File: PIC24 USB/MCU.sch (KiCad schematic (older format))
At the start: 12 parts, among them U1 PIC24FJXXXGB106, X1 CRYSTAL_12MHZ

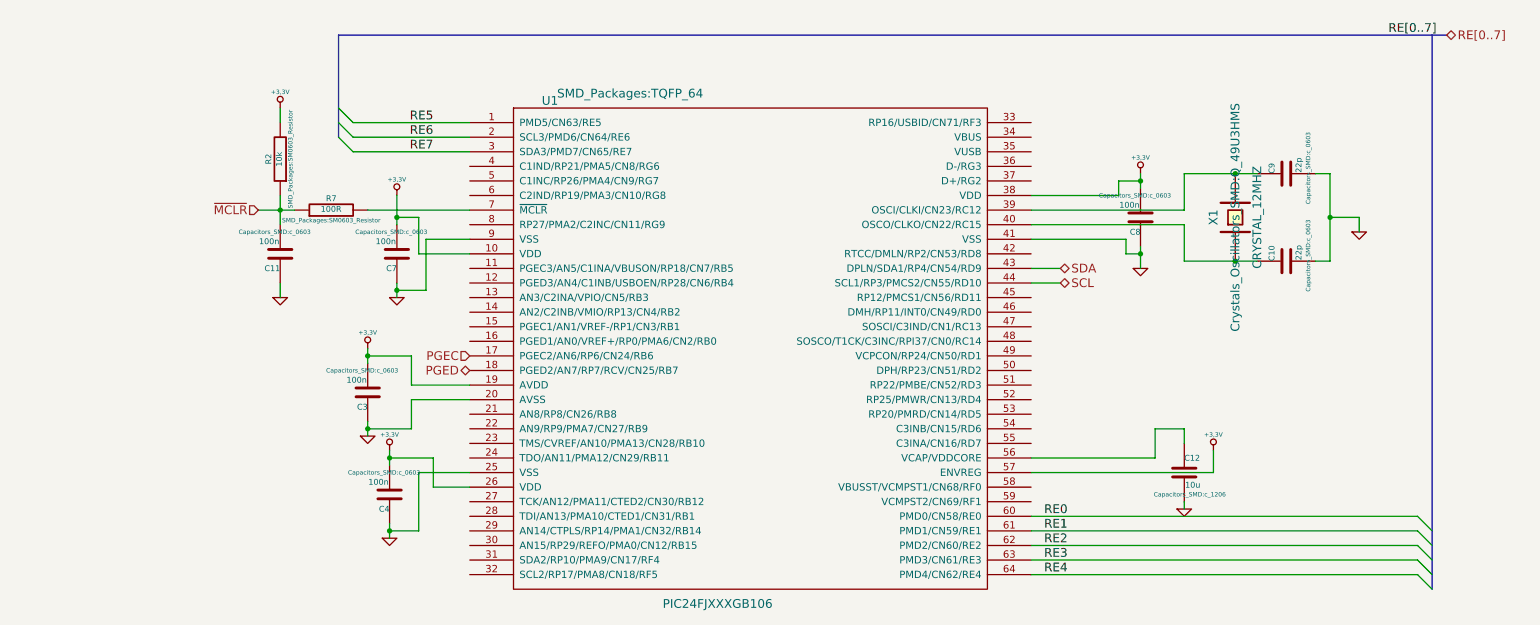
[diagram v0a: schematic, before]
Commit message: added led display, many additional headers and DAC
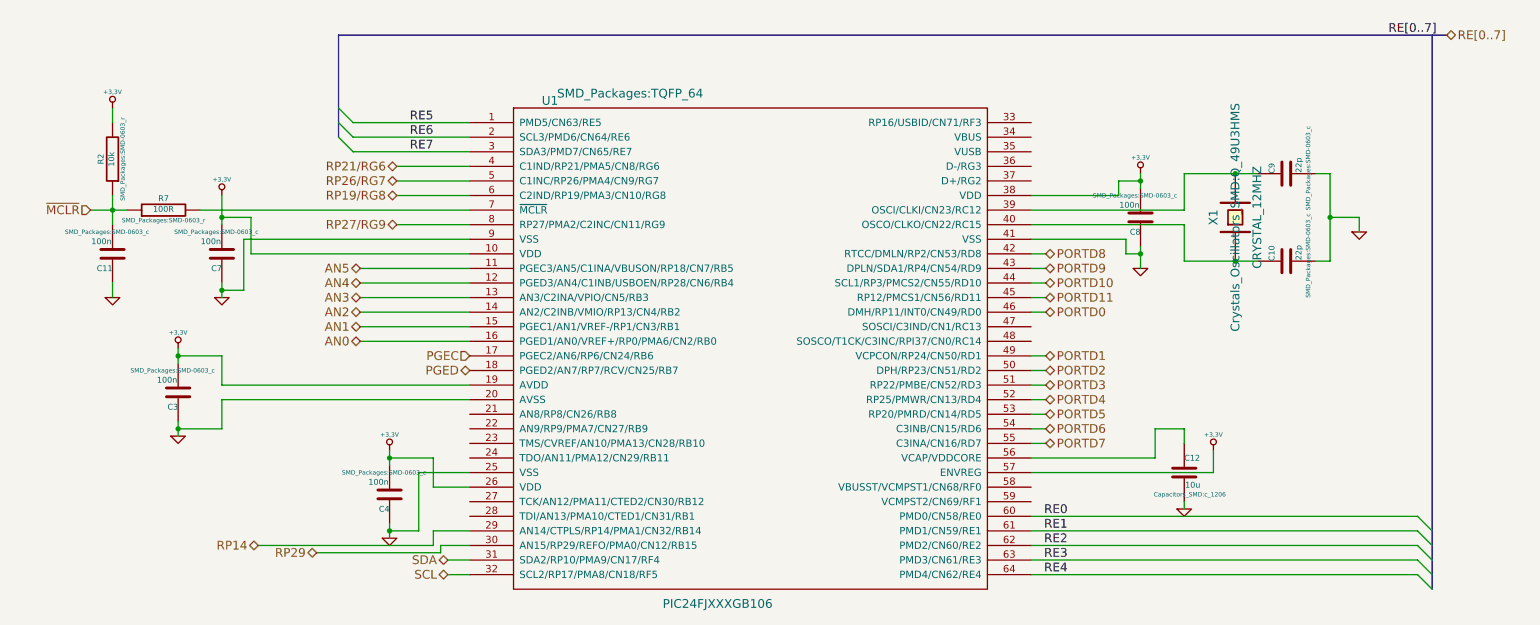
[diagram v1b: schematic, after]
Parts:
- C10, C11, C3, C4, C7, C8, C9: footprint Capacitors_SMD:c_0603 -> SMD_Packages:SMD-0603_c
- R2, R7: footprint SMD_Packages:SM0603_Resistor -> SMD_Packages:SMD-0603_r
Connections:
- net SCL: now also U1.32 (SCL2/RP17/PMA8/CN18/RF5); no longer U1.44 (SCL1/RP3/PMCS2/CN55/RD10)
- net SDA: now also U1.31 (SDA2/RP10/PMA9/CN17/RF4); no longer U1.43 (DPLN/SDA1/RP4/CN54/RD9)
- net AN5: now reaches U1.11 (PGEC3/AN5/C1INA/VBUSON/RP18/CN7/RB5)
- net AN4: now reaches U1.12 (PGED3/AN4/C1INB/USBOEN/RP28/CN6/RB4)
- net AN3: now reaches U1.13 (AN3/C2INA/VPIO/CN5/RB3)
- net AN2: now reaches U1.14 (AN2/C2INB/VMIO/RP13/CN4/RB2)
- net AN1: now reaches U1.15 (PGEC1/AN1/VREF-/RP1/CN3/RB1)
- net AN0: now reaches U1.16 (PGED1/AN0/VREF+/RP0/PMA6/CN2/RB0)
- net RP14: now reaches U1.29 (AN14/CTPLS/RP14/PMA1/CN32/RB14)
- net RP29: now reaches U1.30 (AN15/RP29/REFO/PMA0/CN12/RB15)
- net RP21/RG6: now reaches U1.4 (C1IND/RP21/PMA5/CN8/RG6)
- net PORTD8: now reaches U1.42 (RTCC/DMLN/RP2/CN53/RD8)
- net PORTD11: now reaches U1.45 (RP12/PMCS1/CN56/RD11)
- net PORTD0: now reaches U1.46 (DMH/RP11/INT0/CN49/RD0)
- net PORTD1: now reaches U1.49 (VCPCON/RP24/CN50/RD1)
- net RP26/RG7: now reaches U1.5 (C1INC/RP26/PMA4/CN9/RG7)
- net PORTD2: now reaches U1.50 (DPH/RP23/CN51/RD2)
- net PORTD3: now reaches U1.51 (RP22/PMBE/CN52/RD3)
- net PORTD4: now reaches U1.52 (RP25/PMWR/CN13/RD4)
- net PORTD5: now reaches U1.53 (RP20/PMRD/CN14/RD5)
- net PORTD6: now reaches U1.54 (C3INB/CN15/RD6)
- net PORTD7: now reaches U1.55 (C3INA/CN16/RD7)
- net RP19/RG8: now reaches U1.6 (C2IND/RP19/PMA3/CN10/RG8)
- net RP27/RG9: now reaches U1.8 (RP27/PMA2/C2INC/CN11/RG9)
- new net PORTD10: U1.44 (SCL1/RP3/PMCS2/CN55/RD10)
- new net PORTD9: U1.43 (DPLN/SDA1/RP4/CN54/RD9)
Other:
- moved on the sheet: C11, C3, C7, R2, R7

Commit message: more hierarchical pin for MCU section, connected USB lines in schematic
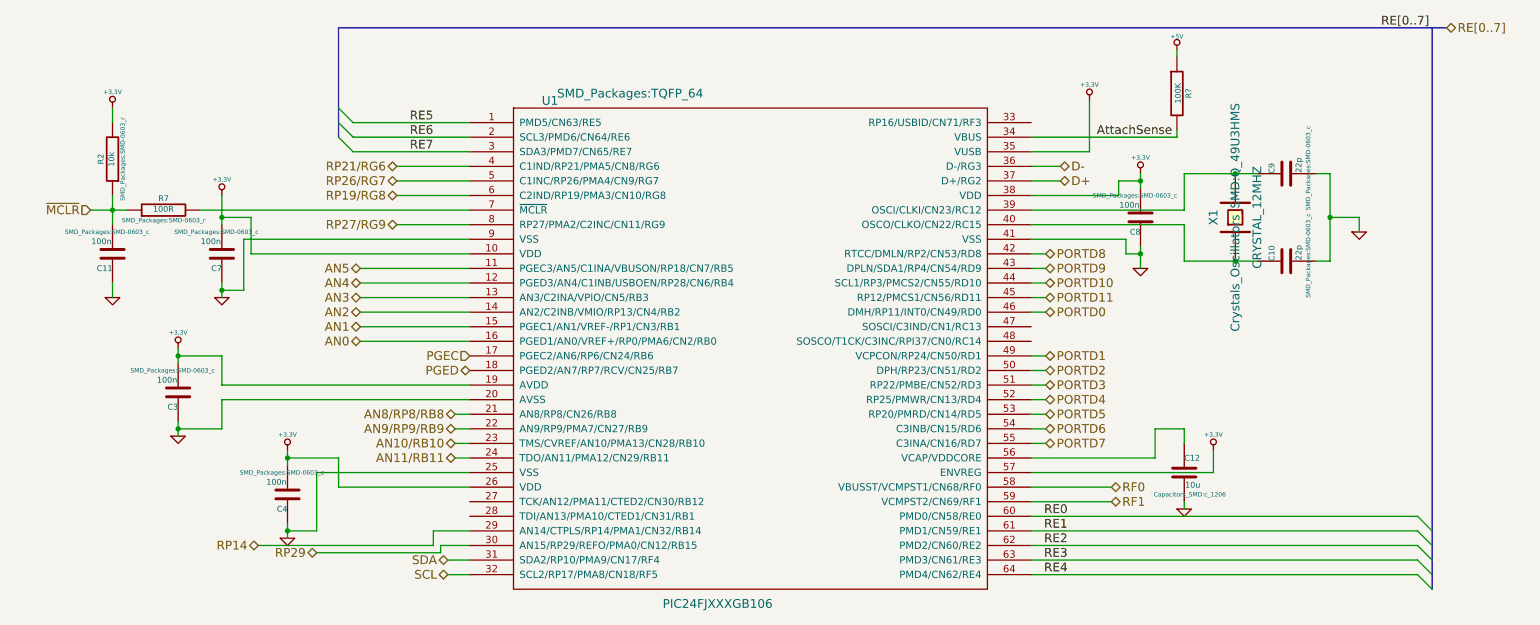
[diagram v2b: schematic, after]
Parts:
- added R?: 100K, symbol R
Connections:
- net +3.3V: now also U1.35 (VUSB)
- net AN8/RP8/RB8: now reaches U1.21 (AN8/RP8/CN26/RB8)
- net AN9/RP9/RB9: now reaches U1.22 (AN9/RP9/PMA7/CN27/RB9)
- net AN10/RB10: now reaches U1.23 (TMS/CVREF/AN10/PMA13/CN28/RB10)
- net AN11/RB11: now reaches U1.24 (TDO/AN11/PMA12/CN29/RB11)
- net AttachSense: now reaches U1.34 (VBUS)
- net AttachSense: now also R?.2
- net D-: now reaches U1.36 (D-/RG3)
- net D+: now reaches U1.37 (D+/RG2)
- net RF0: now reaches U1.58 (VBUSST/VCMPST1/CN68/RF0)
- net RF1: now reaches U1.59 (VCMPST2/CN69/RF1)
- new net +5V: R?.1
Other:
- moved on the sheet: C4

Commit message: connected SPI DAC
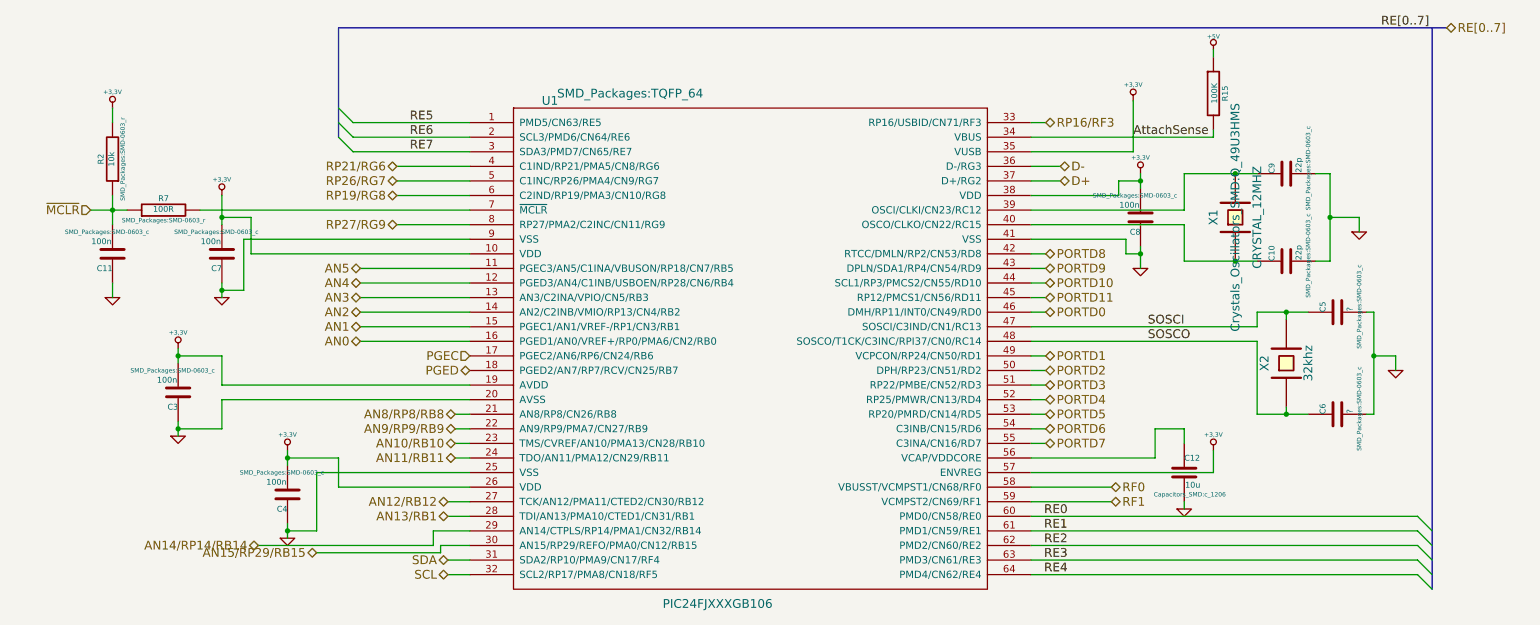
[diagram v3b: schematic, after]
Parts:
- added C5, C6: ?, SMD_Packages:SMD-0603_c, symbol C
- added X2: 32khz, symbol CRYSTAL
- gave numbers to parts that had none: 1
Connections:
- net AttachSense is gone; now on net +3.3V: R15.2, U1.34 (VBUS)
- net GND: now also C5.2, C6.2
- net AN12/RB12: now reaches U1.27 (TCK/AN12/PMA11/CTED2/CN30/RB12)
- net AN13/RB1: now reaches U1.28 (TDI/AN13/PMA10/CTED1/CN31/RB1)
- net RP16/RF3: now reaches U1.33 (RP16/USBID/CN71/RF3)
- net SOSCI: now reaches U1.47 (SOSCI/C3IND/CN1/RC13)
- net SOSCI: now also C5.1, X2.2
- net SOSCO: now reaches U1.48 (SOSCO/T1CK/C3INC/RPI37/CN0/RC14)
- net SOSCO: now also C6.1, X2.1
- net RP14 renamed AN14/RP14/RB14
- net RP29 renamed AN15/RP29/RB15
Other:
- moved on the sheet: R15
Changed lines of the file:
@@
 $Descr A4 11693 8268
 encoding utf-8
-Sheet 2 3
+Sheet 3 3
 Title ""
 Date "3 aug 2014"
@@
 ~MCLR
 $Comp
-L GND #PWR035
+L GND #PWR47
 U 1 1 53DA26E1
 P 1750 3500
-F 0 "#PWR035" H 1750 3500 30  0001 C CNN
+F 0 "#PWR47" H 1750 3500 30  0001 C CNN
 F 1 "GND" H 1750 3430 30  0001 C CNN
 F 2 "" H 1750 3500 60  0000 C CNN
@@
 $EndComp
 $Comp
-L GND #PWR036
+L GND #PWR49
 U 1 1 53DA26EE
 P 2200 5150
-F 0 "#PWR036" H 2200 5150 30  0001 C CNN
+F 0 "#PWR49" H 2200 5150 30  0001 C CNN
 F 1 "GND" H 2200 5080 30  0001 C CNN
 F 2 "" H 2200 5150 60  0000 C CNN
@@
 $EndComp
 $Comp
-L GND #PWR037
+L GND #PWR52
 U 1 1 53DA26F4
 P 8050 3300
-F 0 "#PWR037" H 8050 3300 30  0001 C CNN
+F 0 "#PWR52" H 8050 3300 30  0001 C CNN
 F 1 "GND" H 8050 3230 30  0001 C CNN
 F 2 "" H 8050 3300 60  0000 C CNN
@@
 $EndComp
 $Comp
-L +3,3V #PWR038
+L +3,3V #PWR51
 U 1 1 53DA2840
 P 8050 2650
-F 0 "#PWR038" H 8050 2610 30  0001 C CNN
+F 0 "#PWR51" H 8050 2610 30  0001 C CNN
 F 1 "+3,3V" H 8050 2760 30  0000 C CNN
 F 2 "" H 8050 2650 60  0000 C CNN
@@
 $EndComp
 $Comp
-L +3,3V #PWR039
+L +3,3V #PWR46
 U 1 1 53DA284D
 P 1750 2800
-F 0 "#PWR039" H 1750 2760 30  0001 C CNN
+F 0 "#PWR46" H 1750 2760 30  0001 C CNN
 F 1 "+3,3V" H 1750 2910 30  0000 C CNN
 F 2 "" H 1750 2800 60  0000 C CNN
@@
 $EndComp
 $Comp
-L +3,3V #PWR040
+L +3,3V #PWR48
 U 1 1 53DA2853
 P 2200 4550
-F 0 "#PWR040" H 2200 4510 30  0001 C CNN
+F 0 "#PWR48" H 2200 4510 30  0001 C CNN
 F 1 "+3,3V" H 2200 4660 30  0000 C CNN
 F 2 "" H 2200 4550 60  0000 C CNN
@@
 $EndComp
 $Comp
-L +3,3V #PWR041
+L +3,3V #PWR44
 U 1 1 53DA2865
 P 1450 3850
-F 0 "#PWR041" H 1450 3810 30  0001 C CNN
+F 0 "#PWR44" H 1450 3810 30  0001 C CNN
 F 1 "+3,3V" H 1450 3960 30  0000 C CNN
 F 2 "" H 1450 3850 60  0000 C CNN
@@
 $EndComp
 $Comp
-L GND #PWR042
+L GND #PWR56
 U 1 1 53DA331F
 P 9550 3050
-F 0 "#PWR042" H 9550 3050 30  0001 C CNN
+F 0 "#PWR56" H 9550 3050 30  0001 C CNN
 F 1 "GND" H 9550 2980 30  0001 C CNN
 F 2 "" H 9550 3050 60  0000 C CNN
@@
 $EndComp
 $Comp
-L GND #PWR043
+L GND #PWR45
 U 1 1 53DA3460
 P 1450 4450
-F 0 "#PWR043" H 1450 4450 30  0001 C CNN
+F 0 "#PWR45" H 1450 4450 30  0001 C CNN
 F 1 "GND" H 1450 4380 30  0001 C CNN
 F 2 "" H 1450 4450 60  0000 C CNN
@@
 RE4
 $Comp
-L +3,3V #PWR044
+L +3,3V #PWR55
 U 1 1 53DBFFDE
 P 8550 4550
-F 0 "#PWR044" H 8550 4510 30  0001 C CNN
+F 0 "#PWR55" H 8550 4510 30  0001 C CNN
 F 1 "+3,3V" H 8550 4660 30  0000 C CNN
 F 2 "" H 8550 4550 60  0000 C CNN
@@
 $EndComp
 $Comp
-L GND #PWR045
+L GND #PWR53
 U 1 1 53DC0153
 P 8350 4950
-F 0 "#PWR045" H 8350 4950 30  0001 C CNN
+F 0 "#PWR53" H 8350 4950 30  0001 C CNN
 F 1 "GND" H 8350 4880 30  0001 C CNN
 F 2 "" H 8350 4950 60  0000 C CNN
@@
 $EndComp
 $Comp
-L GND #PWR046
+L GND #PWR43
 U 1 1 53DEB25D
 P 1000 3500
-F 0 "#PWR046" H 1000 3500 30  0001 C CNN
+F 0 "#PWR43" H 1000 3500 30  0001 C CNN
 F 1 "GND" H 1000 3430 30  0001 C CNN
 F 2 "" H 1000 3500 60  0000 C CNN
@@
 $EndComp
 $Comp
-L +3,3V #PWR047
+L +3,3V #PWR42
 U 1 1 53DEB263
 P 1000 2200
-F 0 "#PWR047" H 1000 2160 30  0001 C CNN
+F 0 "#PWR42" H 1000 2160 30  0001 C CNN
 F 1 "+3,3V" H 1000 2310 30  0000 C CNN
 F 2 "" H 1000 2200 60  0000 C CNN
@@
 PORTD11
 Text HLabel 2400 5250 0    60   BiDi ~ 0
-RP29
+AN15/RP29/RB15
 Text HLabel 2000 5200 0    60   BiDi ~ 0
-RP14
+AN14/RP14/RB14
 Text HLabel 2700 3800 0    60   BiDi ~ 0
 AN0
@@
 RP27/RG9
 $Comp
-L +5V #PWR?
+L +5V #PWR54
 U 1 1 53EB0ECB
-P 8300 1800
-F 0 "#PWR?" H 8300 1890 20  0001 C CNN
-F 1 "+5V" H 8300 1890 30  0000 C CNN
-F 2 "" H 8300 1800 60  0000 C CNN
-F 3 "" H 8300 1800 60  0000 C CNN
-	1    8300 1800
-	1    0    0    -1
-$EndComp
-$Comp
-L R R?
+P 8550 1800
+F 0 "#PWR54" H 8550 1890 20  0001 C CNN
+F 1 "+5V" H 8550 1890 30  0000 C CNN
+F 2 "" H 8550 1800 60  0000 C CNN
+F 3 "" H 8550 1800 60  0000 C CNN
+	1    8550 1800
+	1    0    0    -1
+$EndComp
+$Comp
+L R R15
 U 1 1 53EB0F03
-P 8300 2100
-F 0 "R?" V 8380 2100 40  0000 C CNN
-F 1 "100K" V 8307 2101 40  0000 C CNN
-F 2 "" V 8230 2100 30  0000 C CNN
-F 3 "" H 8300 2100 30  0000 C CNN
-	1    8300 2100
+P 8550 2100
+F 0 "R15" V 8630 2100 40  0000 C CNN
+F 1 "100K" V 8557 2101 40  0000 C CNN
+F 2 "" V 8480 2100 30  0000 C CNN
+F 3 "" H 8550 2100 30  0000 C CNN
+	1    8550 2100
 	1    0    0    -1
 $EndComp
@@
 	3450 2600 2950 2600
 Wire Wire Line
-	7300 2400 8300 2400
-Wire Wire Line
-	8300 2400 8300 2350
-Wire Wire Line
-	8300 1850 8300 1800
-Text Label 7750 2400 0    60   ~ 0
+	7300 2400 8550 2400
+Wire Wire Line
+	8550 2400 8550 2350
+Wire Wire Line
+	8550 1850 8550 1800
+Text Label 8000 2400 0    60   ~ 0
 AttachSense
 Wire Wire Line
-	7300 2500 7700 2500
-Wire Wire Line
-	7700 2500 7700 2150
-$Comp
-L +3,3V #PWR?
+	7300 2500 8000 2500
+Wire Wire Line
+	8000 2500 8000 2150
+$Comp
+L +3,3V #PWR50
 U 1 1 53EB1BF4
-P 7700 2150
-F 0 "#PWR?" H 7700 2110 30  0001 C CNN
-F 1 "+3,3V" H 7700 2260 30  0000 C CNN
-F 2 "" H 7700 2150 60  0000 C CNN
-F 3 "" H 7700 2150 60  0000 C CNN
-	1    7700 2150
+P 8000 2150
+F 0 "#PWR50" H 8000 2110 30  0001 C CNN
+F 1 "+3,3V" H 8000 2260 30  0000 C CNN
+F 2 "" H 8000 2150 60  0000 C CNN
+F 3 "" H 8000 2150 60  0000 C CNN
+	1    8000 2150
 	1    0    0    -1
 $EndComp
@@
 Text HLabel 3350 4600 0    60   BiDi ~ 0
 AN11/RB11
+Text HLabel 3300 4900 0    60   BiDi ~ 0
+AN12/RB12
+Wire Wire Line
+	3300 4900 3450 4900
+Text HLabel 3300 5000 0    60   BiDi ~ 0
+AN13/RB1
+Wire Wire Line
+	3300 5000 3450 5000
+Text HLabel 7400 2300 2    60   BiDi ~ 0
+RP16/RF3
+Wire Wire Line
+	7300 2300 7400 2300
+$Comp
+L CRYSTAL X2
+U 1 1 53F4D63C
+P 9050 3950
+F 0 "X2" H 9050 4100 60  0000 C CNN
+F 1 "32khz" H 9050 3800 60  0000 C CNN
+F 2 "" H 9050 3950 60  0000 C CNN
+F 3 "" H 9050 3950 60  0000 C CNN
+	1    9050 3950
+	0    -1   -1   0
+$EndComp
+$Comp
+L C C5
+U 1 1 53F4D6C5
+P 9400 3600
+F 0 "C5" H 9400 3700 40  0000 L CNN
+F 1 "?" H 9406 3515 40  0000 L CNN
+F 2 "SMD_Packages:SMD-0603_c" H 9438 3450 30  0000 C CNN
+F 3 "~" H 9400 3600 60  0000 C CNN
+	1    9400 3600
+	0    -1   -1   0
+$EndComp
+$Comp
+L C C6
+U 1 1 53F4D77C
+P 9400 4300
+F 0 "C6" H 9400 4400 40  0000 L CNN
+F 1 "?" H 9406 4215 40  0000 L CNN
+F 2 "SMD_Packages:SMD-0603_c" H 9438 4150 30  0000 C CNN
+F 3 "~" H 9400 4300 60  0000 C CNN
+	1    9400 4300
+	0    -1   -1   0
+$EndComp
+$Comp
+L GND #PWR57
+U 1 1 53F4D7BA
+P 9800 4000
+F 0 "#PWR57" H 9800 4000 30  0001 C CNN
+F 1 "GND" H 9800 3930 30  0001 C CNN
+F 2 "" H 9800 4000 60  0000 C CNN
+F 3 "" H 9800 4000 60  0000 C CNN
+	1    9800 4000
+	1    0    0    -1
+$EndComp
+Wire Wire Line
+	7300 3700 8850 3700
+Wire Wire Line
+	8850 3700 8850 3600
+Wire Wire Line
+	8850 3600 9200 3600
+Wire Wire Line
+	9050 3650 9050 3600
+Connection ~ 9050 3600
+Wire Wire Line
+	9050 4250 9050 4300
+Wire Wire Line
+	8850 4300 9200 4300
+Wire Wire Line
+	8850 4300 8850 3800
+Wire Wire Line
+	8850 3800 7300 3800
+Connection ~ 9050 4300
+Wire Wire Line
+	9600 3600 9650 3600
+Wire Wire Line
+	9650 3600 9650 4300
+Wire Wire Line
+	9650 4300 9600 4300
+Wire Wire Line
+	9650 3900 9800 3900
+Wire Wire Line
+	9800 3900 9800 4000
+Connection ~ 9650 3900
+Text Label 8100 3700 0    60   ~ 0
+SOSCI
+Text Label 8100 3800 0    60   ~ 0
+SOSCO
 $EndSCHEMATC

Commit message: done a lot of work: ready for submission
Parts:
- R15: footprint (none) -> SMD_Packages:SMD-0603_r
- X2: footprint (none) -> Crystals:Crystal_Round_Horizontal_3mm_BigPad
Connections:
- net +3.3V: no longer R15.2, U1.34 (VBUS)
- new net VBUS_SENSE: R15.2, U1.34 (VBUS)
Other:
- moved on the sheet: R15
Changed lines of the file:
@@
 $EndComp
 $Comp
-L GND #PWR52
+L GND #PWR51
 U 1 1 53DA26F4
 P 8050 3300
-F 0 "#PWR52" H 8050 3300 30  0001 C CNN
+F 0 "#PWR51" H 8050 3300 30  0001 C CNN
 F 1 "GND" H 8050 3230 30  0001 C CNN
 F 2 "" H 8050 3300 60  0000 C CNN
@@
 $EndComp
 $Comp
-L +3,3V #PWR51
+L +3,3V #PWR50
 U 1 1 53DA2840
 P 8050 2650
-F 0 "#PWR51" H 8050 2610 30  0001 C CNN
+F 0 "#PWR50" H 8050 2610 30  0001 C CNN
 F 1 "+3,3V" H 8050 2760 30  0000 C CNN
 F 2 "" H 8050 2650 60  0000 C CNN
@@
 RE4
 $Comp
-L +3,3V #PWR55
+L +3,3V #PWR54
 U 1 1 53DBFFDE
 P 8550 4550
-F 0 "#PWR55" H 8550 4510 30  0001 C CNN
+F 0 "#PWR54" H 8550 4510 30  0001 C CNN
 F 1 "+3,3V" H 8550 4660 30  0000 C CNN
 F 2 "" H 8550 4550 60  0000 C CNN
@@
 $EndComp
 $Comp
-L GND #PWR53
+L GND #PWR52
 U 1 1 53DC0153
 P 8350 4950
-F 0 "#PWR53" H 8350 4950 30  0001 C CNN
+F 0 "#PWR52" H 8350 4950 30  0001 C CNN
 F 1 "GND" H 8350 4880 30  0001 C CNN
 F 2 "" H 8350 4950 60  0000 C CNN
@@
 RP27/RG9
 $Comp
-L +5V #PWR54
+L +5V #PWR53
 U 1 1 53EB0ECB
-P 8550 1800
-F 0 "#PWR54" H 8550 1890 20  0001 C CNN
-F 1 "+5V" H 8550 1890 30  0000 C CNN
-F 2 "" H 8550 1800 60  0000 C CNN
-F 3 "" H 8550 1800 60  0000 C CNN
-	1    8550 1800
+P 8450 1800
+F 0 "#PWR53" H 8450 1890 20  0001 C CNN
+F 1 "+5V" H 8450 1890 30  0000 C CNN
+F 2 "" H 8450 1800 60  0000 C CNN
+F 3 "" H 8450 1800 60  0000 C CNN
+	1    8450 1800
 	1    0    0    -1
 $EndComp
@@
 L R R15
 U 1 1 53EB0F03
-P 8550 2100
-F 0 "R15" V 8630 2100 40  0000 C CNN
-F 1 "100K" V 8557 2101 40  0000 C CNN
-F 2 "" V 8480 2100 30  0000 C CNN
-F 3 "" H 8550 2100 30  0000 C CNN
-	1    8550 2100
+P 8450 2100
+F 0 "R15" V 8530 2100 40  0000 C CNN
+F 1 "100K" V 8457 2101 40  0000 C CNN
+F 2 "SMD_Packages:SMD-0603_r" V 8380 2100 30  0001 C CNN
+F 3 "" H 8450 2100 30  0000 C CNN
+	1    8450 2100
 	1    0    0    -1
 $EndComp
@@
 	3450 2600 2950 2600
 Wire Wire Line
-	7300 2400 8550 2400
-Wire Wire Line
-	8550 2400 8550 2350
-Wire Wire Line
-	8550 1850 8550 1800
-Text Label 8000 2400 0    60   ~ 0
-AttachSense
-Wire Wire Line
-	7300 2500 8000 2500
-Wire Wire Line
-	8000 2500 8000 2150
-$Comp
-L +3,3V #PWR50
+	7300 2400 8450 2400
+Wire Wire Line
+	8450 2400 8450 2350
+Wire Wire Line
+	8450 1850 8450 1800
+Text Label 7900 2400 0    60   ~ 0
+VBUS_SENSE
+Wire Wire Line
+	7300 2500 8650 2500
+Wire Wire Line
+	8650 2500 8650 2150
+$Comp
+L +3,3V #PWR55
 U 1 1 53EB1BF4
-P 8000 2150
-F 0 "#PWR50" H 8000 2110 30  0001 C CNN
-F 1 "+3,3V" H 8000 2260 30  0000 C CNN
-F 2 "" H 8000 2150 60  0000 C CNN
-F 3 "" H 8000 2150 60  0000 C CNN
-	1    8000 2150
+P 8650 2150
+F 0 "#PWR55" H 8650 2110 30  0001 C CNN
+F 1 "+3,3V" H 8650 2260 30  0000 C CNN
+F 2 "" H 8650 2150 60  0000 C CNN
+F 3 "" H 8650 2150 60  0000 C CNN
+	1    8650 2150
 	1    0    0    -1
 $EndComp
@@
 Wire Wire Line
 	3300 5000 3450 5000
-Text HLabel 7400 2300 2    60   BiDi ~ 0
+Text HLabel 7350 2300 2    60   BiDi ~ 0
 RP16/RF3
 Wire Wire Line
-	7300 2300 7400 2300
+	7300 2300 7350 2300
 $Comp
 L CRYSTAL X2
@@
 F 0 "X2" H 9050 4100 60  0000 C CNN
 F 1 "32khz" H 9050 3800 60  0000 C CNN
-F 2 "" H 9050 3950 60  0000 C CNN
+F 2 "Crystals:Crystal_Round_Horizontal_3mm_BigPad" H 9050 3950 60  0001 C CNN
 F 3 "" H 9050 3950 60  0000 C CNN
 	1    9050 3950
